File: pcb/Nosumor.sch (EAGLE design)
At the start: 122 parts, among them IC1 STM32F722RET, J3 SJ-43515TS-SMT-EDGE, K1 CHERRY-MX, K2 CHERRY-MX, K3 KSC623J, K4 KSC623J, K5 KSC623J, Q1 FDY100PZ, Q2 FDY100PZ, Q3 FDY100PZ, Q4 FDY100PZ, Q5 ABMM-6.000MHZ, Q6 CX2016DB, U2 AP2112K-3.3V, U3 USB3370, U4 TLV320AIC3110, U5 AP2112K-1.8V, U6 9DoF IMU

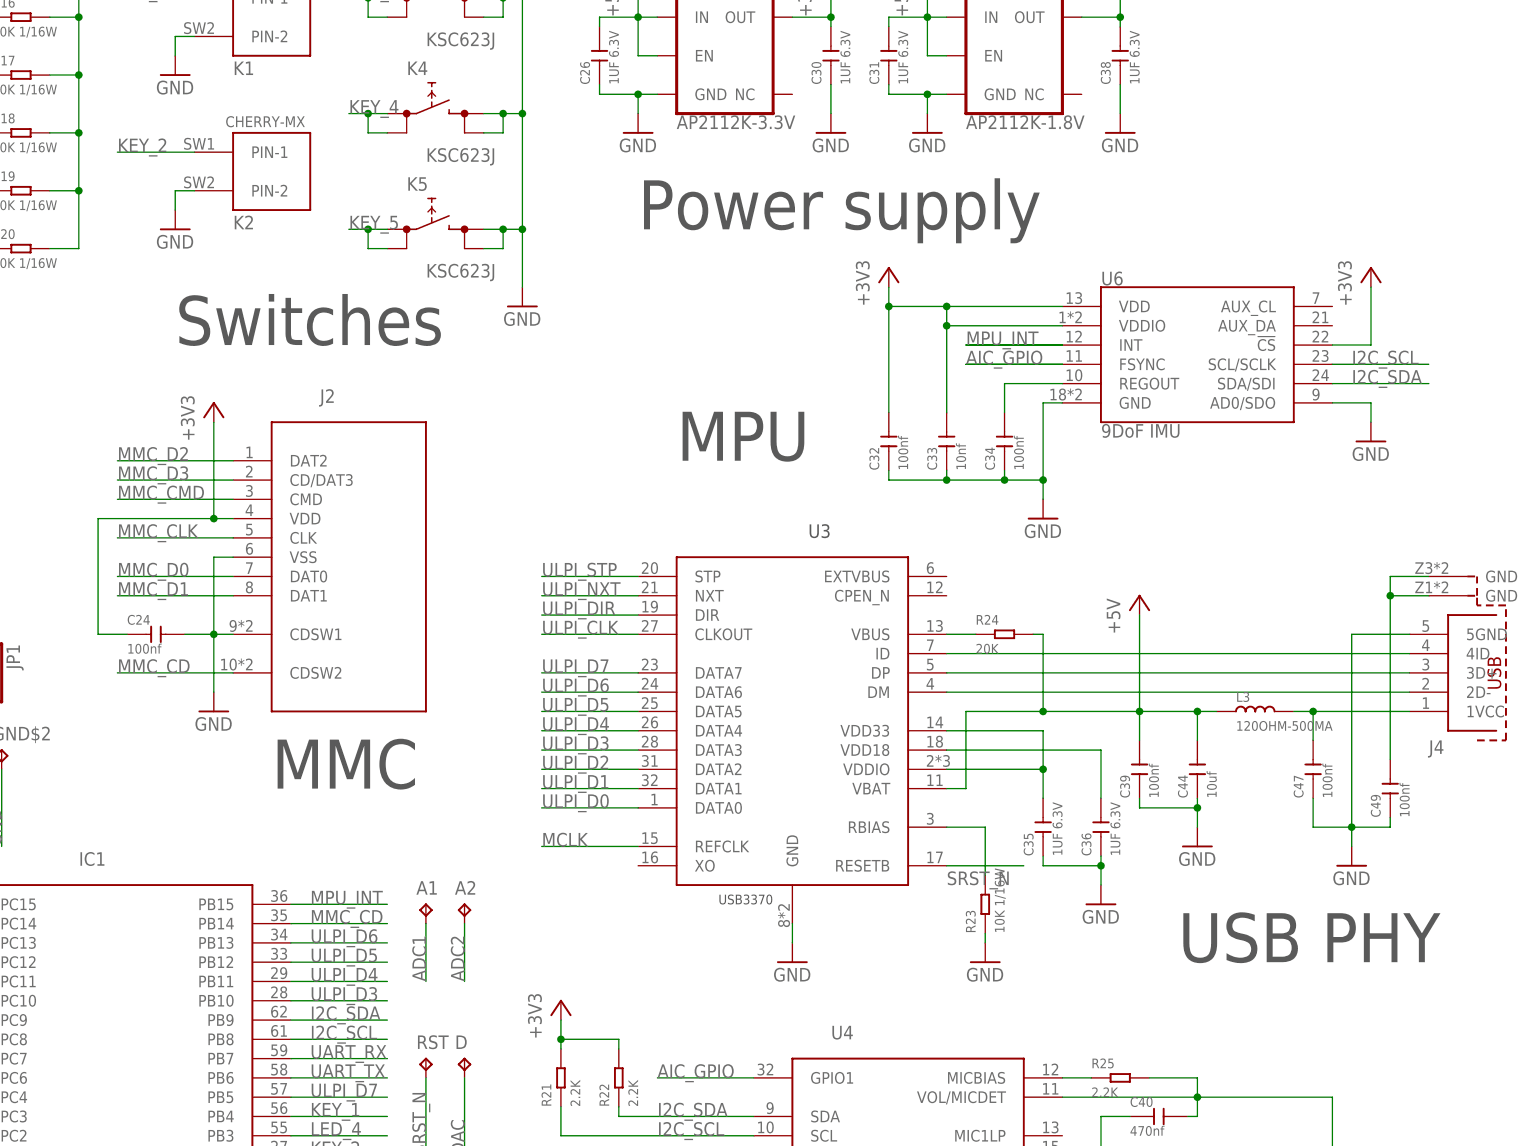
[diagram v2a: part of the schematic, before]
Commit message: PCB: Move a few things around (power supply rails)
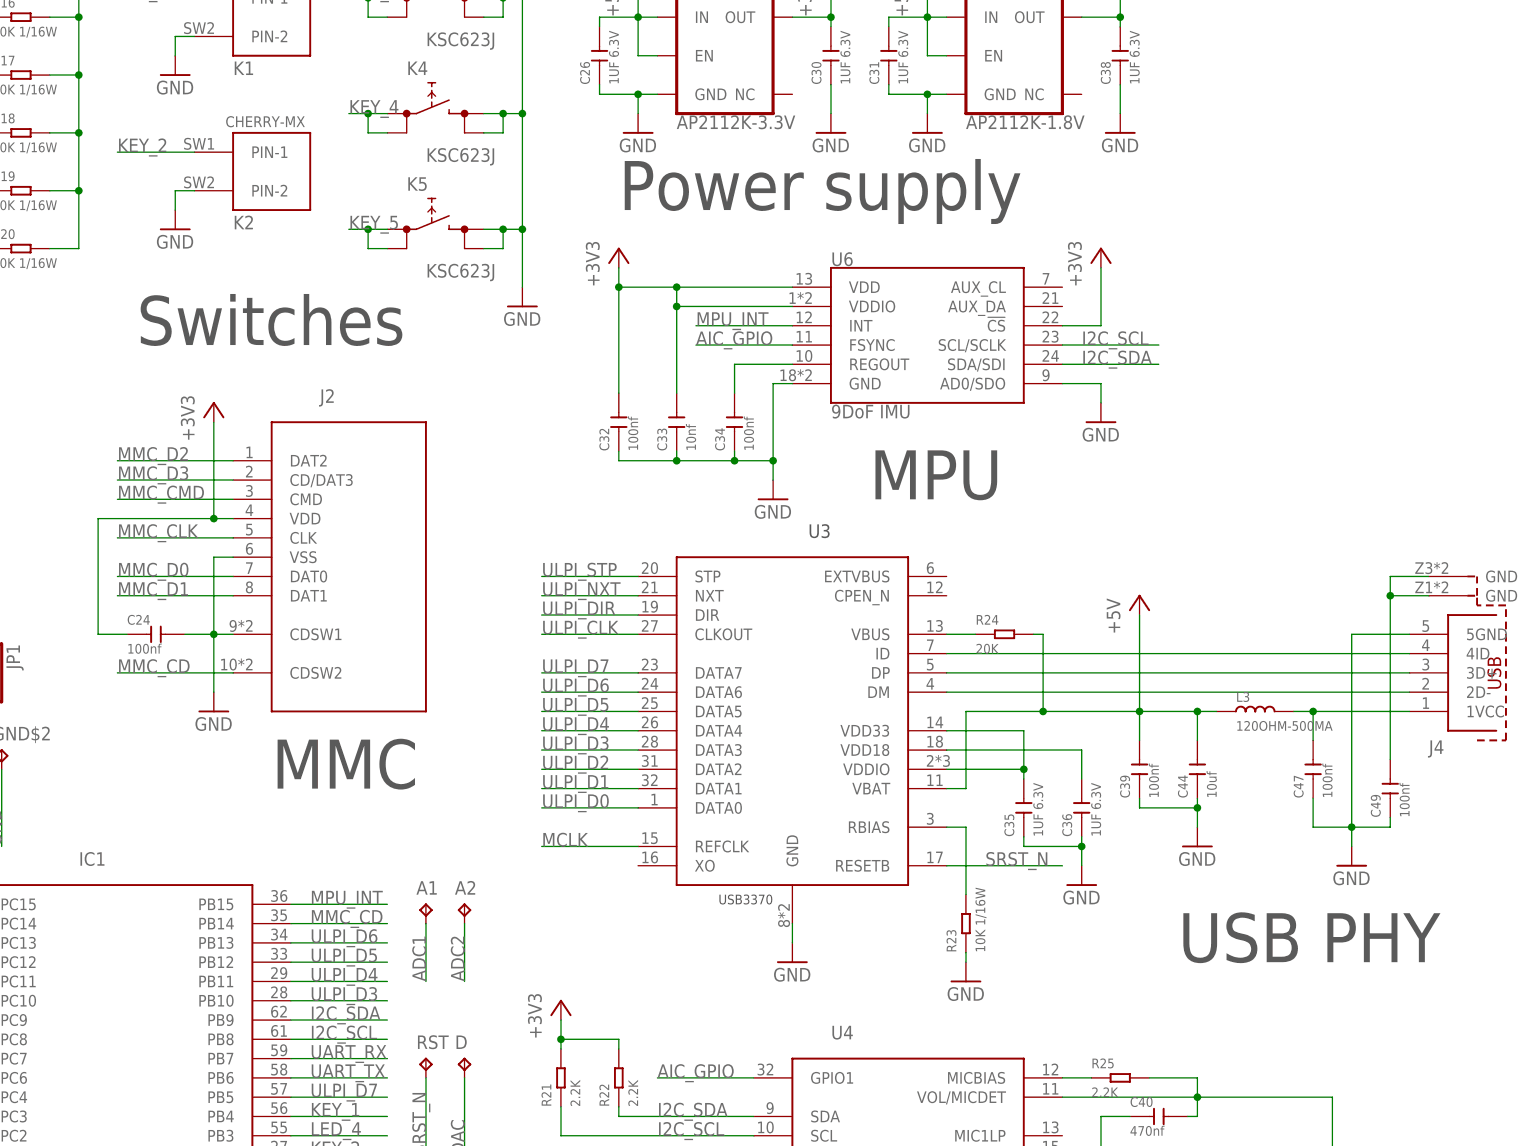
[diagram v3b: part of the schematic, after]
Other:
- moved on the sheet: C32, C33, C34, C35, C36, R23, U6

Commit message: PCB version 1.1 connected
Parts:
- removed D6: MSL0104RGBU1, led:MSL0104RGBU1
- removed JP1: (no value), pinhead:PINHD-1X4
- removed SLM, SLP, SRM, SRP: TPB1,27, testpad:TPB1,27
- added C50, C51: 100nf, Seeed-Capacitor:CERAMIC-100NF-25V-10%-X7R(0402)
- added C52: 1UF 6.3V, Seeed-Capacitor:CERAMIC-1UF-6.3V-10%-X5R(0402)
- added L4: 120OHM-500MA, Seeed-Inductor:SMD-FERRITE-CHIP-120-OHM-500MA(0603)
- added R26: 2k7, Seeed-Resistor:SMD-RES-1K-5%-1/16W(0402)
- added R27, R28: 2k2, Seeed-Resistor:SMD-RES-10K-1%-1/16W(0402)
- added U7: AP2112K-1.8V, SparkFun-IC-Power:V_REG_AP2112K-3.3V
- added U8: 24CW1280T-I/OT, 24CW1280T-I_OT:24CW1280T-I/OT
- C1, C2: value 100nf -> 4p
- C10, C8: value 18pf -> 100nf; device Seeed-Capacitor:CERAMIC-18PF-50V-5%-NPO(0402) -> Seeed-Capacitor:CERAMIC-100NF-25V-10%-X7R(0402)
- C11: value 12pf -> 4u7; device Seeed-Capacitor:CERAMIC-12PF-50V-5%-NPO(0402) -> Seeed-Capacitor:CERAMIC-100NF-25V-10%-X7R(0402)
- C13, C37, C39: value 100nf -> 1UF 6.3V; device Seeed-Capacitor:CERAMIC-100NF-25V-10%-X7R(0402) -> Seeed-Capacitor:CERAMIC-1UF-6.3V-10%-X5R(0402)
- C14, C33: value 10nf -> 100nf; device Seeed-Capacitor:CERAMIC-10NF-50V-10%-X7R(0402) -> Seeed-Capacitor:CERAMIC-100NF-25V-10%-X7R(0402)
- C17, C30, C35: value 1UF 6.3V -> 100nf; device Seeed-Capacitor:CERAMIC-1UF-6.3V-10%-X5R(0402) -> Seeed-Capacitor:CERAMIC-100NF-25V-10%-X7R(0402)
- C18: value 10uf -> 4.7uf; device Seeed-Capacitor:CERAMIC-10UF-10V-10%-X5R(0603) -> Seeed-Capacitor:CERAMIC-4.7UF-10V-10%-X5R(0603)
- C19, C20: value 100nf -> 12pf; device Seeed-Capacitor:CERAMIC-100NF-25V-10%-X7R(0402) -> Seeed-Capacitor:CERAMIC-12PF-50V-5%-NPO(0402)
- C21: value 4.7uf -> 10nf; device Seeed-Capacitor:CERAMIC-4.7UF-10V-10%-X5R(0603) -> Seeed-Capacitor:CERAMIC-10NF-50V-10%-X7R(0402)
- C22: value 10uf -> 1UF 6.3V; device Seeed-Capacitor:CERAMIC-10UF-10V-10%-X5R(0603) -> Seeed-Capacitor:CERAMIC-1UF-6.3V-10%-X5R(0402)
- C25: value 100nf -> 4.7uf; device Seeed-Capacitor:CERAMIC-100NF-25V-10%-X7R(0402) -> Seeed-Capacitor:CERAMIC-4.7UF-10V-10%-X5R(0603)
- C26, C36: value 1UF 6.3V -> 100n; device Seeed-Capacitor:CERAMIC-1UF-6.3V-10%-X5R(0402) -> Seeed-Capacitor:CERAMIC-100NF-25V-10%-X7R(0402)
- C27, C32: value 100nf -> 100n
- C28, C43, C44: value 10uf -> 100nf; device Seeed-Capacitor:CERAMIC-10UF-10V-10%-X5R(0603) -> Seeed-Capacitor:CERAMIC-100NF-25V-10%-X7R(0402)
- C29, C46: value 100nf -> 2u2
- C34: value 100nf -> 100n; device Seeed-Capacitor:CERAMIC-100NF-25V-10%-X7R(0402) -> Seeed-Capacitor:CERAMIC-10NF-50V-10%-X7R(0402)
- C4: value 100nf -> 3u3
- C40: value 470nf -> 1UF 6.3V; device Seeed-Capacitor:CERAMIC-47NF-25V-10%-X7R(0402) -> Seeed-Capacitor:CERAMIC-1UF-6.3V-10%-X5R(0402)
- C41: value 100uf -> 1UF 6.3V; device Seeed-Capacitor:CERAMIC-100UF-6.3V-20%-X5R(1206) -> Seeed-Capacitor:CERAMIC-1UF-6.3V-10%-X5R(0402)
- C42, C48: value 100uf -> 100nf; device Seeed-Capacitor:CERAMIC-100UF-6.3V-20%-X5R(1206) -> Seeed-Capacitor:CERAMIC-100NF-25V-10%-X7R(0402)
- C45, C47: value 100nf -> 10uf; device Seeed-Capacitor:CERAMIC-100NF-25V-10%-X7R(0402) -> Seeed-Capacitor:CERAMIC-10UF-10V-10%-X5R(0603)
- C6: value 4.7uf -> 100nf; device Seeed-Capacitor:CERAMIC-4.7UF-10V-10%-X5R(0603) -> Seeed-Capacitor:CERAMIC-100NF-25V-10%-X7R(0402)
- C7: value 33nf -> 4u7; device Seeed-Capacitor:CERAMIC-22NF-50V-10%-X7R(0402) -> Seeed-Capacitor:CERAMIC-100NF-25V-10%-X7R(0402)
- C9: value 12pf -> 100nf; device Seeed-Capacitor:CERAMIC-12PF-50V-5%-NPO(0402) -> Seeed-Capacitor:CERAMIC-100NF-25V-10%-X7R(0402)
- D1: value APBD3224SURKCGKC-F01 -> MSL0601RGB; device led:APBD3224SURKCGKC-F01 -> led:MSL0601RGB
- D2: value APBD3224SURKCGKC-F01 -> HSMF-A3-BACK; device led:APBD3224SURKCGKC-F01 -> led:HSMF-A3-BACK
- D3, D5: value HSMF-A3-BACK -> MSL0601RGB; device led:HSMF-A3-BACK -> led:MSL0601RGB
- D4: value MSL0104RGBU1 -> HSMF-A3-BACK; device led:MSL0104RGBU1 -> led:HSMF-A3-BACK
- Q1: value FDY100PZ -> ABM8W-12.0000MHZ; device transistor:FDY100PZ -> crystal:ABM8W-12.0000MHZ
- Q5: value ABMM-6.000MHZ -> FDY100PZ; device crystal:ABMM-6.000MHZ -> transistor:FDY100PZ
- R10: value 1.5K -> 150R; device Seeed-Resistor:SMD-RES-1.5K-5%-1/16W(0402) -> Seeed-Resistor:SMD-RES-330R-1%-1/16W(0402)
- R12, R13: value 22R -> 10K 1/16W; device Seeed-Resistor:SMD-RES-22R-1%-1/16W(0402) -> Seeed-Resistor:SMD-RES-10K-1%-1/16W(0402)
- R18, R19, R20: value 10K 1/16W -> 27R; device Seeed-Resistor:SMD-RES-10K-1%-1/16W(0402) -> Seeed-Resistor:SMD-RES-330R-1%-1/16W(0402)
- R2: value 150R -> 330R
- R21, R22: value 2.2K -> 27R; device Seeed-Resistor:SMD-RES-1K-5%-1/16W(0402) -> Seeed-Resistor:SMD-RES-330R-1%-1/16W(0402)
- R23: value 10K 1/16W -> 10R; device Seeed-Resistor:SMD-RES-10K-1%-1/16W(0402) -> Seeed-Resistor:SMD-RES-330R-1%-1/16W(0402)
- R24: value 20K -> 10K 1/16W; device Seeed-Resistor:SMD-RES-1K-5%-1/16W(0402) -> Seeed-Resistor:SMD-RES-10K-1%-1/16W(0402)
- R25: value 2.2K -> 20K
- R4: value 150R -> 12K 1/16W; device Seeed-Resistor:SMD-RES-330R-1%-1/16W(0402) -> Seeed-Resistor:SMD-RES-10K-1%-1/16W(0402)
- R5: value 330R -> 2k2; device Seeed-Resistor:SMD-RES-330R-1%-1/16W(0402) -> Seeed-Resistor:SMD-RES-10K-1%-1/16W(0402)
- R6: value 150R -> 470R 1/16W; device Seeed-Resistor:SMD-RES-330R-1%-1/16W(0402) -> Seeed-Resistor:SMD-RES-470R-5%-1/16W(0402)
- R7: value 330R -> 10K 1/16W; device Seeed-Resistor:SMD-RES-330R-1%-1/16W(0402) -> Seeed-Resistor:SMD-RES-10K-1%-1/16W(0402)
- R8, R9: value 470R 1/16W -> 150R; device Seeed-Resistor:SMD-RES-470R-5%-1/16W(0402) -> Seeed-Resistor:SMD-RES-330R-1%-1/16W(0402)
- U1: value (none) -> FT2232H-56Q-REEL; device ftdichip-6:FT2232L -> FT2232H-56Q-REEL:FT2232H-56Q-REEL
- U3: value USB3370 -> AP2112K-3.3V; device microchip:USB3370 -> SparkFun-IC-Power:V_REG_AP2112K-3.3V
- U4: value TLV320AIC3110 -> USB3370; device ti:TLV320AIC3110 -> microchip:USB3370
- U5: value AP2112K-1.8V -> TLV320AIC3256; device SparkFun-IC-Power:V_REG_AP2112K-3.3V -> ti:TLV320AIC3256
- renumbered A1 to TP4, A2 to TP7, BOOT to SJ1, CLK to TP6, D to TP8, DIO to TP9, GND to TP10, GND$2 to TP3, RST to TP5, SCL to TP2, SDA to TP1, VDD to TP11
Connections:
- removed net AVDD: C28.2, C29.2, C37.2, C43.2, L2.1, U4.AVDD, U4.HPVDD
- removed net DBG_5V: C13.2, C16.2, C18.2, D1GREEN.A, D1RED.A, D2GREEN.A, D2RED.A, L1.1, R11.2, R9.2, U1.RESET#, U1.VCC0, U1.VCC1
- removed net DBG_BM_U: J1.2D-, R12.2
- removed net DBG_DM: R12.1, U1.USBDM
- removed net DBG_DP: R10.2, R13.1, U1.USBDP
- removed net DBG_DP_U: J1.3D+, R13.2
- removed net DBG_SWD_LED1: R5.1, U1.ACBUS2
- removed net DBG_SWD_LED2: R1.1, U1.ACBUS3
- removed net N$10: C7.1, U1.3V3OUT, U1.VCCIOA, U1.VCCIOB
- removed net N$11 (its old number): C2.1, R9.1, U1.AVVC
- removed net N$27: C15.2, J1.GND@1, J1.GND@2
- removed net N$44: SRP.TP, U4.SPRP
- removed net N$45: SRM.TP, U4.SPRM
- removed net N$46: C40.1, U4.MIC1RP
- removed net N$48: C42.1, U4.HPR
- removed net N$49: R25.1, U4.MICBIAS
- removed net N$50: C41.1, U4.HPL
- removed net UART_RX: IC1G$1.PB7, JP1.3
- removed net UART_TX: IC1G$1.PB6, JP1.2
- new net DBG_1V8: C3.2, C4.2, C5.2, U1.VCORE, U1.VREGOUT
- new net DBG_3V3: C10.2, C13.2, C6.2, C8.2, D1.A, L1.2, L2.2, R5.2, R7.2, U1.VCCIO, U1.VREGIN, U2.OUT
- new net DBG_SWD_LED: R3.1, U1.ACBUS3
- new net N$15: R7.1, U1.EEDATA
- new net N$16: D1.KR, R1.2
- new net N$22: R20.2, U5.BCLK
- new net N$39: D2.A, Q3.D
- new net N$40: R23.2, U5.MCLK
- new net N$41: D1.KB, R3.2
- new net N$42: C52.2, J1.1VCC, U2.EN, U2.IN
- new net N$43: J1.3D+, U1.DP
- new net N$51: J1.2D-, U1.DM
- new net N$52: R4.1, U1.REF
- new net N$53: R5.1, U1.!RESET#
- new net N$54: C7.2, C9.2, L1.1, U1.VPHY
- new net N$55: C11.2, C12.2, L2.1, U1.VPLL
- new net N$56: R6.2, U1.ADBUS1
- new net N$8: C2.2, Q1.2, U1.OSCI
- new net N$9: C1.2, Q1.1, U1.OSCO
- net +1V8: now also C33.2, C41.2, C48.1, C49.1, U5.AVDD, U5.DRVDD_HP, U5.DVDD, U5.DVDD_CP, U7.OUT; no longer C27.2, C38.2, U4.DVDD, U5.OUT
- net +3V3: now also C15.2, C16.2, C18.2, C21.2, C26.2, C27.2, C28.1, C34.2, C35.2, C37.2, Q5.S, R12.2, R13.2, R14.2, R27.2, R28.2, U3.OUT, U5.IOVDD, U5.VSYS, U8.VCC; no longer C1.2, C19.2, C24.1, C25.2, C3.2, C33.2, C4.2, C5.2, C6.2, JP1.1, L2.2, Q1.S, R18.2, R19.2, R20.2, R21.2, R22.2, U2.OUT, U4.IOVDD
- net +5V: now also C38.2, C42.2, C47.2, R25.2, U3.EN, U3.IN, U4.VBAT, U7.EN, U7.IN; no longer C26.2, C39.2, C44.2, C45.2, C46.2, C48.2, R24.2, U2.EN, U2.IN, U3.VBAT, U4.SPLVDD, U4.SPRVDD, U5.EN, U5.IN
- net AIC_BCLK: now also R20.1; no longer U4.BCLK
- net AIC_DIN: now also R19.1; no longer U4.DIN
- net AIC_DOUT: now also R21.1; no longer U4.DOUT
- net AIC_GPIO: now also IC1G$1.PB7, R18.1; no longer U4.GPIO1, U6.FSYNC
- net AIC_WCLK: now also R22.1; no longer U4.WCLK
- net BOOT0: now also R11.1; no longer R14.1
- net DBG_RX_LED: now also R2.1, U1.BCBUS3; no longer R7.1, U1.BCBUS2
- net DBG_TX_LED: now also R1.1, U1.BCBUS4; no longer R3.1, U1.BCBUS3
- net GND: now also C2.1, C24.1, C28.2, C40.1, C41.1, C42.1, C44.2, C45.2, C48.2, C49.2, C50.1, C51.1, C52.1, C7.1, J1.GND@1, J1.GND@2, L4.2, R11.2, R24.1, R4.2, U1.EXP, U1.GND, U4.GND, U5.AVSS, U5.DVSS, U5.DVSS_CP, U5.IOVSS, U5.PAD, U5.SPI_SELECT, U7.GND, U8.VSS; no longer C2.2, C24.2, C28.1, C43.1, C44.1, C45.1, C46.1, C48.1, C49.1, C7.2, J3.4, JP1.4, R14.2, R23.1, U1.AGND, U1.GND0, U1.GND1, U1.GND2, U1.GND3, U4.AVSS, U4.DVSS, U4.HPVSS, U4.IOVSS, U4.SPLVSS, U4.SPRVSS, U5.GND
- net I2C_SCL: now also R28.1, U5.SCL/SSZ, U8.SCL; no longer R21.1, U4.SCL
- net I2C_SDA: now also R27.1, U5.SDA/MOSI, U8.SDA; no longer R22.1, U4.SDA
- net KEY_1: now also R13.1; no longer R16.1
- net KEY_2: now also R14.1; no longer R17.1
- net KEY_3: now also R15.1; no longer R18.1
- net KEY_4: now also R16.1; no longer R19.1
- net KEY_5: now also R17.1; no longer R20.1
- net LED_1: now also Q4.G; no longer Q3.G
- net LED_2: now also Q3.G; no longer Q2.G
- net LED_3: now also Q2.G; no longer Q1.G
- net LED_4: now also Q5.G; no longer Q4.G
- net LED_B: now also R8.1; no longer R2.1
- net LED_G: now also R10.1; no longer R6.1
- net LED_R: now also R9.1; no longer R4.1
- net MCLK: now also R23.1, U4.REFCLK; no longer U3.REFCLK, U4.MCLK
- net MPU_INT: now also IC1G$1.PB6; no longer IC1G$1.PB15
- net N$1: now also R22.2, U5.WCLK; no longer C41.2, J3.2
- net N$12: now also J3.3, U5.HPR; no longer D1GREEN.C, R5.2
- net N$13: now also J3.2, U5.HPL; no longer C12.2, J1.1VCC, L1.2
- net N$14: now also J3.4, L4.1, U5.GND_SENSE; no longer R10.1, U1.RSTOUT#
- net N$17: now also C43.2, J3.1, R26.2, U5.MICDET; no longer R11.1, U1.EEDATA
- net N$18: now also R26.1, U5.MICBIAS; no longer C8.2, Q5.1, U1.XTOUT
- net N$19: now also C43.1, U5.IN1_L; no longer C10.2, Q5.2, U1.XTIN
- net N$2: now also R19.2, U5.DIN/MFP1; no longer C42.2, J3.3
- net N$20: now also C44.1, U5.IN1_R, U5.IN2_L, U5.IN2_R, U5.IN3_L, U5.IN3_R; no longer D2GREEN.C, R7.2
- net N$21: now also C45.1, U5.REF; no longer D2RED.C, R3.2
- net N$23: now also C46.1, U5.FLY_N; no longer D1RED.C, R1.2
- net N$24: now also C19.2; no longer C9.2
- net N$25: now also C46.2, U5.FLY_P; no longer R8.2, U1.ADBUS1
- net N$26: now also C20.2; no longer C11.2
- net N$28: now also D5.A, Q5.D; no longer D6.AB, D6.AG, D6.AR1, D6.AR2, Q4.D
- net N$29: now also C25.2; no longer C21.2
- net N$3: now also R21.2, U5.DOUT/MFP2; no longer C40.2, J3.1, R25.2, U4.VOL/MICDET
- net N$30: now also D1.KG, R2.2; no longer SLM.TP, U4.SPLM
- net N$31: now also C50.2; no longer C47.2
- net N$32: now also R25.1, U4.VBUS; no longer R24.1, U3.VBUS
- net N$33: now also C39.2, U4.VDD33, U4.VDDIO; no longer C35.2, U3.VDD33, U3.VDDIO
- net N$34: now also D4.A, Q4.D; no longer D5.A, Q3.D
- net N$35: now also C51.2; no longer C49.2
- net N$36: now also C40.2, U4.VDD18; no longer C36.2, U3.VDD18
- net N$37: now also R24.2, U4.RBIAS; no longer R23.2, U3.RBIAS
- net N$38: now also C29.2, U5.VNEG; no longer D4.AB, D4.AG, D4.AR1, D4.AR2, Q1.D
- net N$4: now also U4.DM; no longer U3.DM
- net N$47: now also C36.2; no longer C34.2
- net N$5: now also U4.DP; no longer U3.DP
- net N$6: now also U4.ID; no longer U3.ID
- net N$7: now also R18.2, U5.GPIO/MFP5; no longer SLP.TP, U4.SPLP
- net RGB_B: now also D2.KB, D4.KB, R8.2; no longer D4.KG, D6.KG, R2.2
- net RGB_G: now also D2.KG, D4.KG, R10.2; no longer D4.KB, D6.KB, R6.2
- net RGB_R: now also D2.KR, R9.2; no longer D6.KR, R4.2
- net SRST_N: now also C24.2, R12.1, U4.RESETB, U5.!RESET; no longer C20.2, R15.1, U3.RESETB, U4.!RESET
- net SWDIO: now also R6.1; no longer R8.1
- net ULPI_CLK: now also U4.CLKOUT; no longer U3.CLKOUT
- net ULPI_D0: now also U4.DATA0; no longer U3.DATA0
- net ULPI_D1: now also U4.DATA1; no longer U3.DATA1
- net ULPI_D2: now also U4.DATA2; no longer U3.DATA2
- net ULPI_D3: now also U4.DATA3; no longer U3.DATA3
- net ULPI_D4: now also U4.DATA4; no longer U3.DATA4
- net ULPI_D5: now also U4.DATA5; no longer U3.DATA5
- net ULPI_D6: now also U4.DATA6; no longer U3.DATA6
- net ULPI_D7: now also U4.DATA7; no longer U3.DATA7
- net ULPI_DIR: now also U4.DIR; no longer U3.DIR
- net ULPI_NXT: now also U4.NXT; no longer U3.NXT
- net ULPI_STP: now also U4.STP; no longer U3.STP
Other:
- moved on the sheet: C1, C10, C11, C12, C13, C14, C15, C16, C17, C18, C19, C2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

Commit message: PCB with silkscreen
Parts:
- removed L4: 120OHM-500MA, Seeed-Inductor:SMD-FERRITE-CHIP-120-OHM-500MA(0603)
- C1, C2: value 4p -> 4u7; device Seeed-Capacitor:CERAMIC-100NF-25V-10%-X7R(0402) -> Seeed-Capacitor:CERAMIC-1UF-6.3V-10%-X5R(0402)
- C13, C31, C37: value 1UF 6.3V -> 100n; device Seeed-Capacitor:CERAMIC-1UF-6.3V-10%-X5R(0402) -> Seeed-Capacitor:CERAMIC-100NF-25V-10%-X7R(0402)
- C15, C33: value 100nf -> 100n; device Seeed-Capacitor:CERAMIC-100NF-25V-10%-X7R(0402) -> Seeed-Capacitor:CERAMIC-10NF-50V-10%-X7R(0402)
- C16: value 100nf -> 4u7
- C18: value 4.7uf -> 100nf; device Seeed-Capacitor:CERAMIC-4.7UF-10V-10%-X5R(0603) -> Seeed-Capacitor:CERAMIC-100NF-25V-10%-X7R(0402)
- C19: value 12pf -> 100nf; device Seeed-Capacitor:CERAMIC-12PF-50V-5%-NPO(0402) -> Seeed-Capacitor:CERAMIC-100NF-25V-10%-X7R(0402)
- C20: value 12pf -> 100n; device Seeed-Capacitor:CERAMIC-12PF-50V-5%-NPO(0402) -> Seeed-Capacitor:CERAMIC-100NF-25V-10%-X7R(0402)
- C21: value 10nf -> 4u7; device Seeed-Capacitor:CERAMIC-10NF-50V-10%-X7R(0402) -> Seeed-Capacitor:CERAMIC-100NF-25V-10%-X7R(0402)
- C22, C40, C41, C52: value 1UF 6.3V -> 100nf; device Seeed-Capacitor:CERAMIC-1UF-6.3V-10%-X5R(0402) -> Seeed-Capacitor:CERAMIC-100NF-25V-10%-X7R(0402)
- C23, C35, C43, C44, C5, C6: value 100nf -> 4u7; device Seeed-Capacitor:CERAMIC-100NF-25V-10%-X7R(0402) -> Seeed-Capacitor:CERAMIC-1UF-6.3V-10%-X5R(0402)
- C24, C8: value 100nf -> 100n
- C25: value 4.7uf -> 4u7; device Seeed-Capacitor:CERAMIC-4.7UF-10V-10%-X5R(0603) -> Seeed-Capacitor:CERAMIC-1UF-6.3V-10%-X5R(0402)
- C26: value 100n -> 100nf
- C28, C30: value 100nf -> 12pf; device Seeed-Capacitor:CERAMIC-100NF-25V-10%-X7R(0402) -> Seeed-Capacitor:CERAMIC-12PF-50V-5%-NPO(0402)
- C29: value 2u2 -> 100n
- C34: value 100n -> 4u7; device Seeed-Capacitor:CERAMIC-10NF-50V-10%-X7R(0402) -> Seeed-Capacitor:CERAMIC-4.7UF-10V-10%-X5R(0603)
- C38: value 1UF 6.3V -> 4u7; device Seeed-Capacitor:CERAMIC-1UF-6.3V-10%-X5R(0402) -> Seeed-Capacitor:CERAMIC-4.7UF-10V-10%-X5R(0603)
- C39: value 1UF 6.3V -> 2u2; device Seeed-Capacitor:CERAMIC-1UF-6.3V-10%-X5R(0402) -> rcl:C-EUC0603K
- C4: value 3u3 -> 4u7; device Seeed-Capacitor:CERAMIC-100NF-25V-10%-X7R(0402) -> Seeed-Capacitor:CERAMIC-1UF-6.3V-10%-X5R(0402)
- C45: value 10uf -> 4u7; device Seeed-Capacitor:CERAMIC-10UF-10V-10%-X5R(0603) -> Seeed-Capacitor:CERAMIC-1UF-6.3V-10%-X5R(0402)
- C46: value 2u2 -> 100nf
- C47: value 10uf -> 2u2; device Seeed-Capacitor:CERAMIC-10UF-10V-10%-X5R(0603) -> rcl:C-EUC0603K
- C50: value 100nf -> 10uf; device Seeed-Capacitor:CERAMIC-100NF-25V-10%-X7R(0402) -> Seeed-Capacitor:CERAMIC-10UF-10V-10%-X5R(0603)
- C7: value 4u7 -> 4p
- C9: value 100nf -> 4p
- D3: value MSL0601RGB -> HSMF-A3-BACK; device led:MSL0601RGB -> led:HSMF-A3-BACK
- D4: value HSMF-A3-BACK -> MSL0601RGB; device led:HSMF-A3-BACK -> led:MSL0601RGB
- J3: value SJ-43515TS-SMT-EDGE -> (none); device connector:SJ-43515TS-SMT-EDGE -> Wurth_Elektronik_Electromechanic_Input-Output_Connectors_rev16b:629105150521
- J4: value (none) -> SJ-43515TS-SMT-EDGE; device Wurth_Elektronik_Electromechanic_Input-Output_Connectors_rev16b:629105150521 -> connector:SJ-43515TS-SMT-EDGE
- Q2: value FDY100PZ -> CX2016DB; device transistor:FDY100PZ -> crystal:CX2016DB
- Q6: value CX2016DB -> FDY100PZ; device crystal:CX2016DB -> transistor:FDY100PZ
- R10: value 150R -> 10K 1/16W; device Seeed-Resistor:SMD-RES-330R-1%-1/16W(0402) -> Seeed-Resistor:SMD-RES-10K-1%-1/16W(0402)
- R12, R13, R14: value 10K 1/16W -> 100R; device Seeed-Resistor:SMD-RES-10K-1%-1/16W(0402) -> Seeed-Resistor:SMD-RES-330R-1%-1/16W(0402)
- R15, R16, R17: value 10K 1/16W -> 27R; device Seeed-Resistor:SMD-RES-10K-1%-1/16W(0402) -> Seeed-Resistor:SMD-RES-330R-1%-1/16W(0402)
- R20: value 27R -> 10R
- R21, R22: value 27R -> 10K 1/16W; device Seeed-Resistor:SMD-RES-330R-1%-1/16W(0402) -> Seeed-Resistor:SMD-RES-10K-1%-1/16W(0402)
- R23: value 10R -> 10K 1/16W; device Seeed-Resistor:SMD-RES-330R-1%-1/16W(0402) -> Seeed-Resistor:SMD-RES-10K-1%-1/16W(0402)
- R25: value 20K -> 10K 1/16W; device Seeed-Resistor:SMD-RES-1K-5%-1/16W(0402) -> Seeed-Resistor:SMD-RES-10K-1%-1/16W(0402)
- R26: value 2k7 -> 10K 1/16W; device Seeed-Resistor:SMD-RES-1K-5%-1/16W(0402) -> Seeed-Resistor:SMD-RES-10K-1%-1/16W(0402)
- R27: value 2k2 -> 20K; device Seeed-Resistor:SMD-RES-10K-1%-1/16W(0402) -> Seeed-Resistor:SMD-RES-1K-5%-1/16W(0402)
- R28: value 2k2 -> 2k7; device Seeed-Resistor:SMD-RES-10K-1%-1/16W(0402) -> Seeed-Resistor:SMD-RES-1K-5%-1/16W(0402)
- R4: value 12K 1/16W -> 12k 1%
- R6: value 470R 1/16W -> 330R
- R8, R9: value 150R -> 2k2; device Seeed-Resistor:SMD-RES-330R-1%-1/16W(0402) -> Seeed-Resistor:SMD-RES-10K-1%-1/16W(0402)
- U1: value FT2232H-56Q-REEL -> 3.3V; device FT2232H-56Q-REEL:FT2232H-56Q-REEL -> SparkFun-IC-Power:V_REG_AP2112K-3.3V
- U2: value AP2112K-3.3V -> FT2232H-56Q-REEL; device SparkFun-IC-Power:V_REG_AP2112K-3.3V -> FT2232H-56Q-REEL:FT2232H-56Q-REEL
- U3: value AP2112K-3.3V -> 3.3V
- U4: value USB3370 -> 24CW1280T-I/OT; device microchip:USB3370 -> 24CW1280T-I_OT:24CW1280T-I/OT
- U5: value TLV320AIC3256 -> 9DoF IMU; device ti:TLV320AIC3256 -> SparkFun-Sensors:MPU-9250
- U6: value 9DoF IMU -> 3.3V; device SparkFun-Sensors:MPU-9250 -> SparkFun-IC-Power:V_REG_AP2112K-3.3V
- U7: value AP2112K-1.8V -> USB3370; device SparkFun-IC-Power:V_REG_AP2112K-3.3V -> microchip:USB3370
- U8: value 24CW1280T-I/OT -> TLV320AIC3256; device 24CW1280T-I_OT:24CW1280T-I/OT -> ti:TLV320AIC3256
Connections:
- removed net N$31: C50.2, J4.1VCC, L3.2
- removed net N$34 (its old number): D4.A, Q4.D
- removed net N$35: C51.2, J4.GND@1, J4.GND@2
- new net N$39: D3.A, Q4.D
- net +1V8: now also C51.1, C52.1, C6.2, U3.OUT, U8.AVDD, U8.DRVDD_HP, U8.DVDD, U8.DVDD_CP; no longer C33.2, C48.1, C49.1, U5.AVDD, U5.DRVDD_HP, U5.DVDD, U5.DVDD_CP, U7.OUT
- net +3V3: now also C13.2, C2.2, C24.2, C29.2, C3.1, C31.2, C33.2, C36.2, C4.2, C40.2, C42.2, C8.2, Q6.S, R11.2, R21.2, R22.2, R23.2, R24.2, R25.2, R8.2, R9.2, TP8.TP, U1.OUT, U4.VCC, U5.!CS, U5.VDD, U5.VDDIO, U8.IOVDD, U8.VSYS; no longer C14.2, C16.2, C17.2, C18.2, C21.2, C22.2, C23.2, C26.2, C28.1, C30.2, C37.2, Q2.S, R12.2, R13.2, R14.2, R15.2, R16.2, R17.2, R27.2, R28.2, TP11.TP, U3.OUT, U5.IOVDD, U5.VSYS, U6.!CS, U6.VDD, U6.VDDIO, U8.VCC
- net +5V: now also C1.2, C45.2, C48.2, C5.2, J3.1VCC, R27.2, U1.EN, U1.IN, U7.VBAT; no longer C31.2, C38.2, C42.2, C47.2, L3.1, R25.2, U4.VBAT, U7.EN, U7.IN
- net ADC1: now also TP6.TP; no longer TP4.TP
- net ADC2: now also TP10.TP; no longer TP7.TP
- net AIC_BCLK: now also R17.1; no longer R20.1
- net AIC_DIN: now also R16.1; no longer R19.1
- net AIC_DOUT: now also R18.1; no longer R21.1
- net AIC_GPIO: now also R15.1; no longer R18.1
- net AIC_WCLK: now also R19.1; no longer R22.1
- net BOOT0: now also R10.1; no longer R11.1
- net DAC: now also TP2.TP; no longer TP8.TP
- net DBG_1V8: now also C10.2, C11.2, C12.2, U2.VCORE, U2.VREGOUT; no longer C3.2, C4.2, C5.2, U1.VCORE, U1.VREGOUT
- net DBG_3V3: now also C14.2, C17.2, C19.2, C23.2, U2.VCCIO, U2.VREGIN, U6.OUT; no longer C10.2, C13.2, C6.2, C8.2, U1.VCCIO, U1.VREGIN, U2.OUT
- net DBG_RXD: now also U2.BDBUS1; no longer U1.BDBUS1
- net DBG_RX_LED: now also U2.BCBUS3; no longer U1.BCBUS3
- net DBG_SWD_LED: now also U2.ACBUS3; no longer U1.ACBUS3
- net DBG_TXD: now also U2.BDBUS0; no longer U1.BDBUS0
- net DBG_TX_LED: now also U2.BCBUS4; no longer U1.BCBUS4
- net GND: now also C28.1, C3.2, C39.2, C43.1, C44.1, C45.1, C48.1, C50.2, C51.2, C52.2, J3.5GND, J3.GND@1, J3.GND@2, L3.2, R10.2, R26.1, TP4.TP, TP9.TP, U2.EXP, U2.TEST, U4.VSS, U5.AD0/SDO, U5.GND, U8.AVSS, U8.DVSS, U8.DVSS_CP, U8.IOVSS, U8.PAD, U8.SPI_SELECT; no longer C28.2, C3.1, C39.1, C44.2, C45.2, C47.1, C48.2, C50.1, C51.1, C52.1, J4.5GND, L4.2, R11.2, R24.1, TP10.TP, TP3.TP, U1.EXP, U1.TEST, U4.GND, U5.AVSS, U5.DVSS, U5.DVSS_CP, U5.IOVSS, U5.PAD, U5.SPI_SELECT, U6.AD0/SDO, U8.VSS
- net I2C_SCL: now also R8.1, TP5.TP, U4.SCL, U5.SCL/SCLK, U8.SCL/SSZ; no longer R28.1, TP2.TP, U5.SCL/SSZ, U6.SCL/SCLK, U8.SCL
- net I2C_SDA: now also R9.1, U4.SDA, U5.SDA/SDI, U8.SDA/MOSI; no longer R27.1, U5.SDA/MOSI, U6.SDA/SDI, U8.SDA
- net KEY_1: now also R21.1; no longer R13.1
- net KEY_2: now also R22.1; no longer R14.1
- net KEY_3: now also R23.1; no longer R15.1
- net KEY_4: now also R24.1; no longer R16.1
- net KEY_5: now also R25.1; no longer R17.1
- net LED_1: now also Q3.G; no longer Q4.G
- net LED_2: now also Q4.G; no longer Q3.G
- net LED_3: now also Q5.G; no longer Q2.G
- net LED_4: now also Q6.G; no longer Q5.G
- net LED_B: now also R14.1; no longer R8.1
- net LED_G: now also R13.1; no longer R10.1
- net LED_R: now also R12.1; no longer R9.1
- net MCLK: now also R20.1, U7.REFCLK; no longer R23.1, U4.REFCLK
- net MPU_INT: now also U5.INT; no longer U6.INT
- net N$1: now also R19.2, U8.WCLK; no longer R22.2, U5.WCLK
- net N$11: now also D4.A, Q5.D; no longer D3.A, Q2.D
- net N$12: now also J4.3, U8.HPR; no longer J3.3, U5.HPR
- net N$13: now also J4.2, U8.HPL; no longer J3.2, U5.HPL
- net N$14: now also J4.4, L3.1, U8.GND_SENSE; no longer J3.4, L4.1, U5.GND_SENSE
- net N$15: now also U2.EEDATA; no longer U1.EEDATA
- net N$17: now also C46.2, J4.1, R28.2, U8.MICDET; no longer C43.2, J3.1, R26.2, U5.MICDET
- net N$18: now also R28.1, U8.MICBIAS; no longer R26.1, U5.MICBIAS
- net N$19: now also C46.1, U8.IN1_L; no longer C43.1, U5.IN1_L
- net N$2: now also R16.2, U8.DIN/MFP1; no longer R19.2, U5.DIN/MFP1
- net N$20: now also C49.1, U8.IN1_R, U8.IN2_L, U8.IN2_R, U8.IN3_L, U8.IN3_R; no longer C44.1, U5.IN1_R, U5.IN2_L, U5.IN2_R, U5.IN3_L, U5.IN3_R
- net N$21: now also C50.1, U8.REF; no longer C45.1, U5.REF
- net N$22: now also R17.2, U8.BCLK; no longer R20.2, U5.BCLK
- net N$23: now also C47.1, U8.FLY_N; no longer C46.1, U5.FLY_N
- net N$24: now also C28.2, Q2G$1.1; no longer C19.2, Q6G$1.1
- net N$25: now also C47.2, U8.FLY_P; no longer C46.2, U5.FLY_P
- net N$26: now also C30.2, Q2G$1.2; no longer C20.2, Q6G$1.2
- net N$28: now also Q6.D; no longer Q5.D
- net N$29: now also C38.2; no longer C25.2
- net N$3: now also R18.2, U8.DOUT/MFP2; no longer R21.2, U5.DOUT/MFP2
- net N$32: now also R27.1, U7.VBUS; no longer R25.1, U4.VBUS
- net N$33: now also C43.2, U7.VDD33, U7.VDDIO; no longer C39.2, U4.VDD33, U4.VDDIO
- net N$36: now also C44.2, U7.VDD18; no longer C40.2, U4.VDD18
- net N$37: now also R26.2, U7.RBIAS; no longer R24.2, U4.RBIAS
- net N$38: now also C39.1, U8.VNEG; no longer C29.2, U5.VNEG
- net N$4: now also J3.2D-, U7.DM; no longer J4.2D-, U4.DM
- net N$40: now also R20.2, U8.MCLK; no longer R23.2, U5.MCLK
- net N$42: now also C25.2, C26.2, U6.EN, U6.IN; no longer C52.2, U2.EN, U2.IN
- net N$43: now also U2.DP; no longer U1.DP
- net N$47: now also C20.2, U5.REGOUT; no longer C36.2, U6.REGOUT
- net N$5: now also J3.3D+, U7.DP; no longer J4.3D+, U4.DP
- net N$51: now also U2.DM; no longer U1.DM
- net N$52: now also U2.REF; no longer U1.REF
- net N$53: now also U2.!RESET#; no longer U1.!RESET#
- net N$54: now also C16.2, C18.2, U2.VPHY; no longer C7.2, C9.2, U1.VPHY
- net N$55: now also C21.2, C22.2, U2.VPLL; no longer C11.2, C12.2, U1.VPLL
- net N$56: now also U2.ADBUS1; no longer U1.ADBUS1
- net N$6: now also J3.4ID, U7.ID; no longer J4.4ID, U4.ID
- net N$7: now also R15.2, U8.GPIO/MFP5; no longer R18.2, U5.GPIO/MFP5
- net N$8: now also C9.2, U2.OSCI; no longer C2.2, U1.OSCI
- net N$9: now also C7.2, U2.OSCO; no longer C1.2, U1.OSCO
- net NRST_N: now also U2.ADBUS7; no longer U1.ADBUS7
- net RGB_B: now also R14.2; no longer R8.2
- net RGB_G: now also R13.2; no longer R10.2
- net RGB_R: now also R12.2; no longer R9.2
- net SRST_N: now also C37.2, R11.1, TP11.TP, U2.ADBUS6, U7.RESETB, U8.!RESET; no longer C24.2, R12.1, TP5.TP, U1.ADBUS6, U4.RESETB, U5.!RESET
- net SWCLK: now also TP3.TP, U2.ADBUS0; no longer TP6.TP, U1.ADBUS0
- net SWDIO: now also TP7.TP, U2.ADBUS2; no longer TP9.TP, U1.ADBUS2
- net ULPI_CLK: now also U7.CLKOUT; no longer U4.CLKOUT
- net ULPI_D0: now also U7.DATA0; no longer U4.DATA0
- net ULPI_D1: now also U7.DATA1; no longer U4.DATA1
- net ULPI_D2: now also U7.DATA2; no longer U4.DATA2
- net ULPI_D3: now also U7.DATA3; no longer U4.DATA3
- net ULPI_D4: now also U7.DATA4; no longer U4.DATA4
- net ULPI_D5: now also U7.DATA5; no longer U4.DATA5
- net ULPI_D6: now also U7.DATA6; no longer U4.DATA6
- net ULPI_D7: now also U7.DATA7; no longer U4.DATA7
- net ULPI_DIR: now also U7.DIR; no longer U4.DIR
- net ULPI_NXT: now also U7.NXT; no longer U4.NXT
- net ULPI_STP: now also U7.STP; no longer U4.STP
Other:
- note added: "Designer: Norman Zhi Date: 2019-03-12"
- note added: "EEPROM"
- note added: "Unnamed USB peripheral"
- moved on the sheet: C1, C10, C11, C12, C13, C14, C15, C16, C17, C18, C19, C2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
